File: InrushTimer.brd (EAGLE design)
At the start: 62.2 x 36 mm, 71 parts, among them IC1 TLC272D, IC2 555, IC3 4076N, Q2 TRANSISTOR-FET_2N7002, Q3 TRANSISTOR-FET_2N7002, Q4 TRANSISTOR-FET_2N7002, Q5 TRANSISTOR-FET_2N7002, Q6 DIODES_ZTX451DIODES_ZTX451_0_0, T1 MMBTA05, U1 ROHM_BY_ELEMENT14_BATCH_1_BU4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

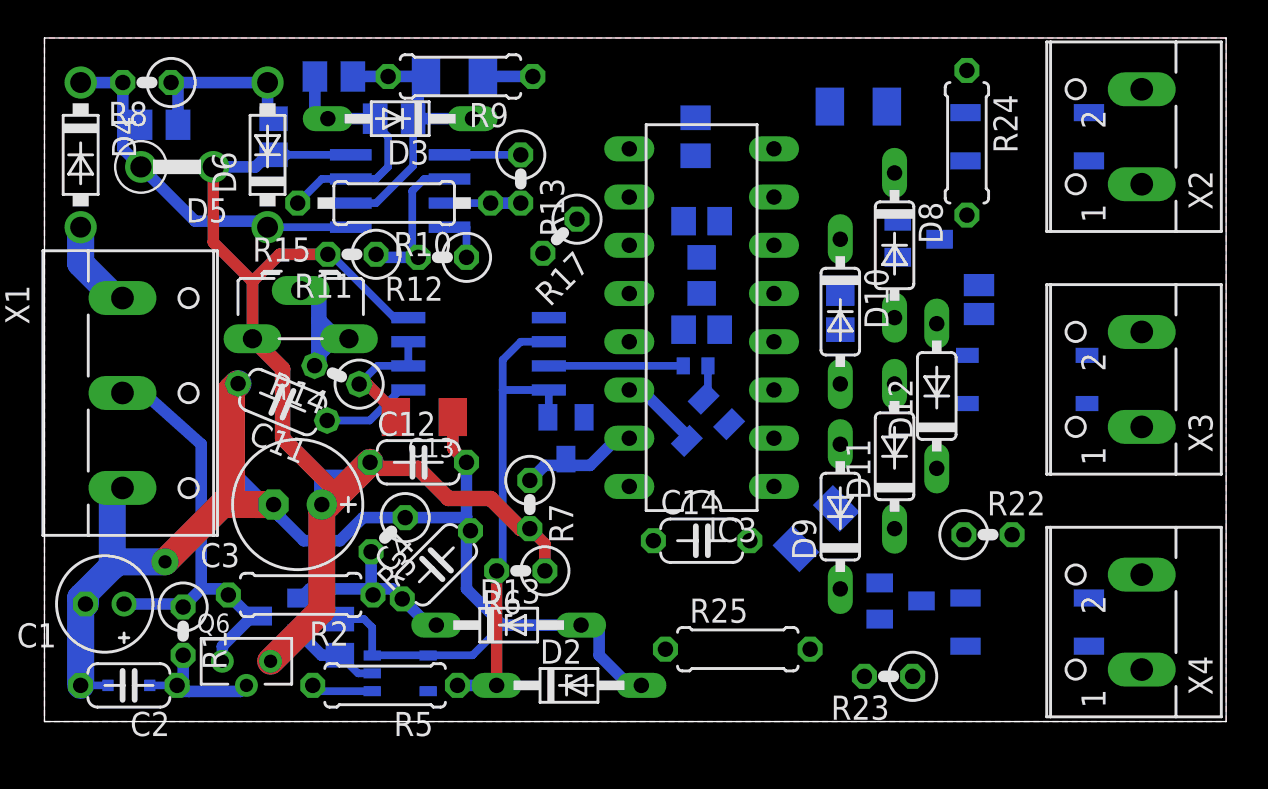
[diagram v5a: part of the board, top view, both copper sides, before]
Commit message: First complete routing fit. Passes design rules.
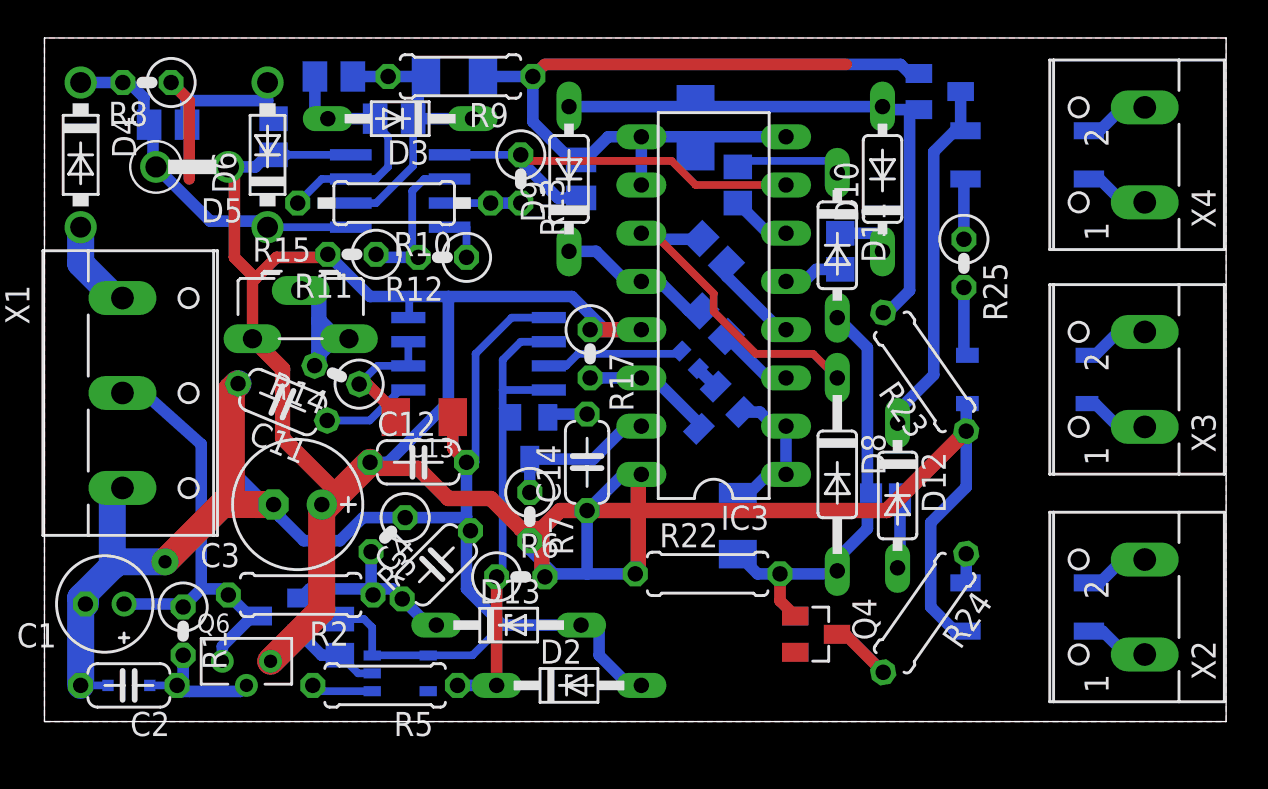
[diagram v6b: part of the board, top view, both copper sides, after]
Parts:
- D8: value 1N4148DO35-7 -> 1N4148DO35-10; device diode:DO35-7 -> diode:DO35-10
- R22, R23: device rcl:0207/2V -> rcl:0207/7
- R25: device rcl:0207/7 -> rcl:0207/2V
- moved Q5 26.9 mm to (47.1, 33.2)
- moved R24 24.9 mm to (46.4, 5.71), turned to 235 degrees
- moved X2 24.8 mm to (56.7, 6.03)
- moved OP1 24.8 mm to (51.8, 6.03)
- moved X4 24.6 mm to (56.7, 29.8)
- moved OP3 24.6 mm to (51.8, 29.8)
- moved R25 23.6 mm to (48.4, 24.1), turned to 270 degrees
- moved C15 23.0 mm to (36.5, 10.3), turned to 270 degrees
- moved D9 22.8 mm to (27.6, 28.6)
- moved C16 22.0 mm to (34.3, 31.3), turned to 270 degrees
- moved Q4 21.5 mm to (40.6, 4.60), flipped to the top, turned to 270 degrees
- moved R23 16.1 mm to (46.4, 18.4), turned to 125 degrees
- moved R22 14.9 mm to (34.9, 7.78)
- moved D8 12.4 mm to (41.8, 13.0)
- moved SJ1 11.6 mm to (44.3, 11.7), turned to 180 degrees
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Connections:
- net N$15: now also R25.1; no longer R25.2
- net N$16: now also IC3.12; no longer IC3.13
- net N$17: now also R25.2; no longer R25.1
- net N$20: now also X3.1; no longer X3.2
- net N$21: now also X3.2; no longer X3.1
- net N$22: now also R19.1; no longer R20.1
- net N$30: now also R20.1; no longer R19.1
- net RESET_N: now also R6.1; no longer R6.2
- net V12: now also IC3.13, R6.2; no longer IC3.12, R6.1
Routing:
- net ZERO: track 97.2 -> 181.3 mm
- net V12: track 87.6 -> 154.9 mm
- net ON_B_SYNC: track 0.00 -> 30.3 mm
- net ON_A_SYNC: track 0.00 -> 23.2 mm
- net N$6: track 0.00 -> 19.4 mm
- net PEAK: track 3.75 -> 22.7 mm
- net N$22: track 0.00 -> 17.5 mm
- net N$16: track 0.00 -> 8.25 mm
- net N$24: track 0.00 -> 6.01 mm
- net N$25: track 0.00 -> 4.94 mm
- net N$32: track 0.00 -> 4.04 mm
- net DISABLE_A: track 0.00 -> 3.70 mm
- net N$17: track 0.00 -> 3.65 mm
- net N$20: track 0.00 -> 3.55 mm
- net N$21: track 0.00 -> 3.55 mm
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
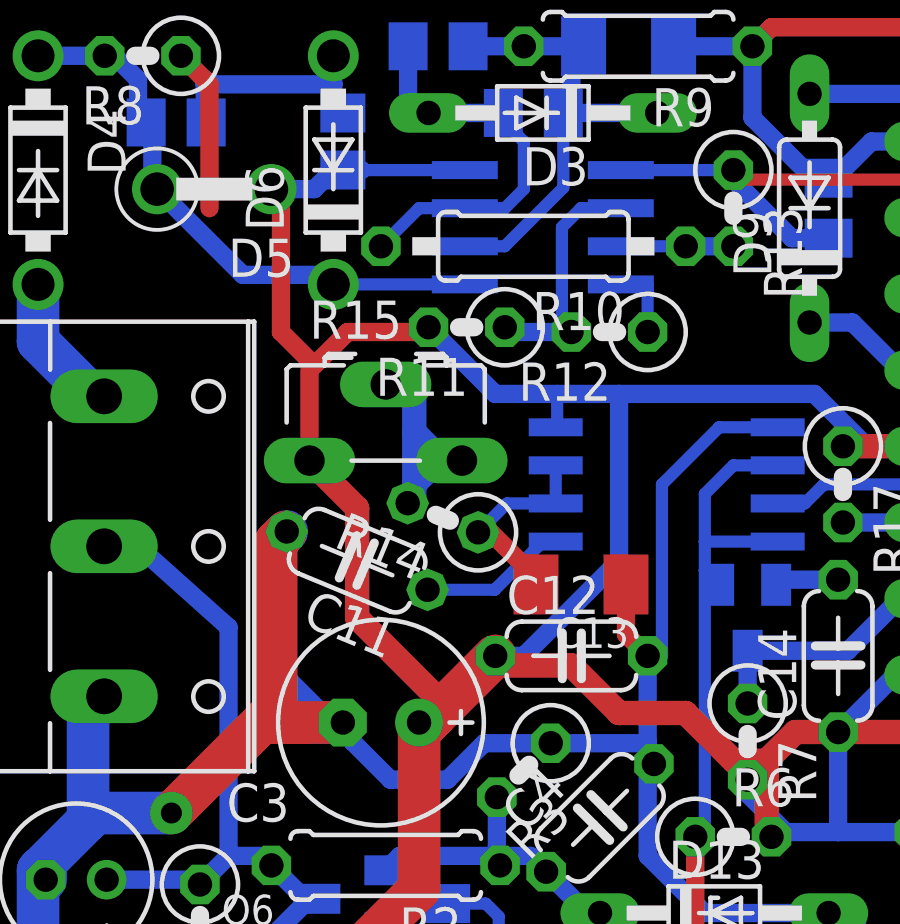
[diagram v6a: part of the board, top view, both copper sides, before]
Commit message: Slight track style tweaks.
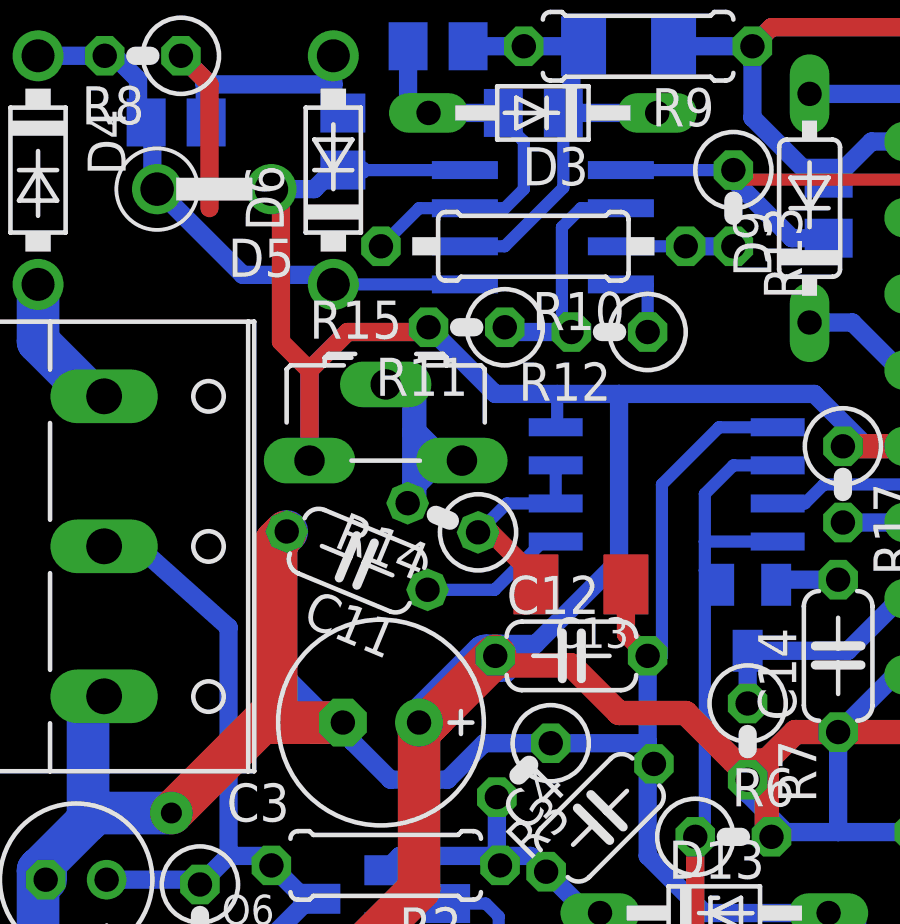
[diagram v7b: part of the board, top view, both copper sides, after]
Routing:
- net V12: track 154.9 -> 156.3 mm
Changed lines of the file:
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@@
 <layer number="39" name="tKeepout" color="4" fill="11" visible="no" active="yes"/>
 <layer number="40" name="bKeepout" color="1" fill="11" visible="no" active="yes"/>
-<layer number="41" name="tRestrict" color="4" fill="10" visible="no" active="yes"/>
+<layer number="41" name="tRestrict" color="4" fill="10" visible="yes" active="yes"/>
 <layer number="42" name="bRestrict" color="1" fill="10" visible="yes" active="yes"/>
 <layer number="43" name="vRestrict" color="2" fill="10" visible="no" active="yes"/>
@@
 <rectangle x1="49.53" y1="0" x2="62.23" y2="36" layer="42"/>
 <rectangle x1="49.53" y1="0" x2="62.23" y2="36" layer="41"/>
-<rectangle x1="0" y1="20.0025" x2="6.35" y2="36" layer="41"/>
+<rectangle x1="0" y1="19.05" x2="6.35" y2="36" layer="41"/>
 <rectangle x1="0" y1="19.05" x2="9.144" y2="30.48" layer="42"/>
 </plain>
@@
 <wire x1="14.605" y1="11.1125" x2="14.9225" y2="11.43" width="1.4224" layer="1"/>
 <wire x1="14.9225" y1="11.43" x2="15.08125" y2="11.58875" width="1.4224" layer="1"/>
-<wire x1="15.08125" y1="11.58875" x2="15.478125" y2="11.985625" width="1.4224" layer="1"/>
-<wire x1="15.478125" y1="11.985625" x2="17.145" y2="13.6525" width="1.4224" layer="1"/>
+<wire x1="15.08125" y1="11.58875" x2="17.145" y2="13.6525" width="1.4224" layer="1"/>
 <wire x1="14.605" y1="11.43" x2="14.9225" y2="11.43" width="1.4224" layer="1"/>
 <wire x1="14.76375" y1="11.58875" x2="15.08125" y2="11.58875" width="0.6096" layer="1"/>
 <contactref element="R15" pad="A"/>
-<wire x1="12.54125" y1="18.57375" x2="12.54125" y2="14.9225" width="0.8128" layer="1"/>
-<wire x1="12.54125" y1="14.9225" x2="15.478125" y2="11.985625" width="0.8128" layer="1"/>
 <contactref element="R7" pad="2"/>
-<wire x1="10.95375" y1="20.16125" x2="12.54125" y2="18.57375" width="0.8128" layer="1"/>
 <wire x1="15.08125" y1="24.60625" x2="14.9225" y2="24.60625" width="0.4064" layer="16"/>
 <wire x1="17.145" y1="13.6525" x2="17.4625" y2="13.335" width="0.8128" layer="1"/>
@@
 <wire x1="31.4325" y1="20.6375" x2="28.73375" y2="20.6375" width="0.8128" layer="1"/>
 <wire x1="21.2725" y1="16.8275" x2="21.2725" y2="22.38375" width="0.6096" layer="16"/>
-<wire x1="21.2725" y1="16.8275" x2="18.0975" y2="13.6525" width="0.6096" layer="16"/>
-<wire x1="14.605" y1="11.43" x2="16.8275" y2="13.6525" width="0.8128" layer="16"/>
-<wire x1="18.0975" y1="13.6525" x2="17.145" y2="13.6525" width="0.6096" layer="16"/>
+<wire x1="21.2725" y1="16.8275" x2="18.494375" y2="14.049375" width="0.6096" layer="16"/>
 <wire x1="48.540325" y1="12.345325" x2="46.6725" y2="10.4775" width="0.6096" layer="16"/>
 <wire x1="46.6725" y1="6.0325" x2="47.9425" y2="4.7625" width="0.6096" layer="16"/>
@@
 <wire x1="25.0825" y1="10.16" x2="26.19375" y2="10.16" width="0.8128" layer="1"/>
 <wire x1="9.68375" y1="29.21" x2="10.00125" y2="29.21" width="0.6096" layer="1"/>
-<wire x1="10.00125" y1="29.21" x2="10.00125" y2="24.4475" width="0.6096" layer="1"/>
+<wire x1="10.00125" y1="29.21" x2="10.00125" y2="24.13" width="0.6096" layer="1"/>
 <wire x1="14.9225" y1="24.60625" x2="14.76375" y2="24.4475" width="0.6096" layer="1"/>
 <wire x1="14.76375" y1="24.4475" x2="12.22375" y2="24.4475" width="0.6096" layer="1"/>
-<wire x1="12.22375" y1="24.4475" x2="11.1125" y2="23.33625" width="0.6096" layer="1"/>
-<wire x1="10.00125" y1="24.4475" x2="11.1125" y2="23.33625" width="0.6096" layer="1"/>
+<wire x1="12.22375" y1="24.4475" x2="10.95375" y2="23.1775" width="0.6096" layer="1"/>
 <wire x1="10.95375" y1="23.1775" x2="10.95375" y2="20.16125" width="0.6096" layer="1"/>
+<wire x1="14.9225" y1="24.60625" x2="14.76375" y2="24.4475" width="0.6096" layer="16"/>
+<wire x1="14.76375" y1="24.4475" x2="12.22375" y2="24.4475" width="0.6096" layer="16"/>
+<wire x1="10.95375" y1="23.1775" x2="10.95375" y2="20.16125" width="0.6096" layer="16"/>
+<wire x1="16.8275" y1="13.6525" x2="17.30375" y2="13.6525" width="1.4224" layer="16"/>
+<wire x1="16.98625" y1="14.049375" x2="18.494375" y2="14.049375" width="0.6096" layer="16"/>
+<wire x1="18.494375" y1="14.049375" x2="17.541875" y2="13.096875" width="0.6096" layer="16"/>
+<wire x1="17.541875" y1="13.096875" x2="17.30375" y2="13.096875" width="0.6096" layer="16"/>
+<wire x1="17.30375" y1="13.096875" x2="16.271875" y2="13.096875" width="0.6096" layer="16"/>
+<wire x1="16.8275" y1="13.6525" x2="14.605" y2="11.43" width="1.4224" layer="16"/>
+<wire x1="10.00125" y1="24.13" x2="10.95375" y2="23.1775" width="0.6096" layer="1"/>
+<wire x1="12.22375" y1="24.4475" x2="10.95375" y2="23.1775" width="0.6096" layer="16"/>
+<wire x1="17.30375" y1="13.6525" x2="17.30375" y2="13.096875" width="0.6096" layer="16"/>
 </signal>
 <signal name="ZERO">

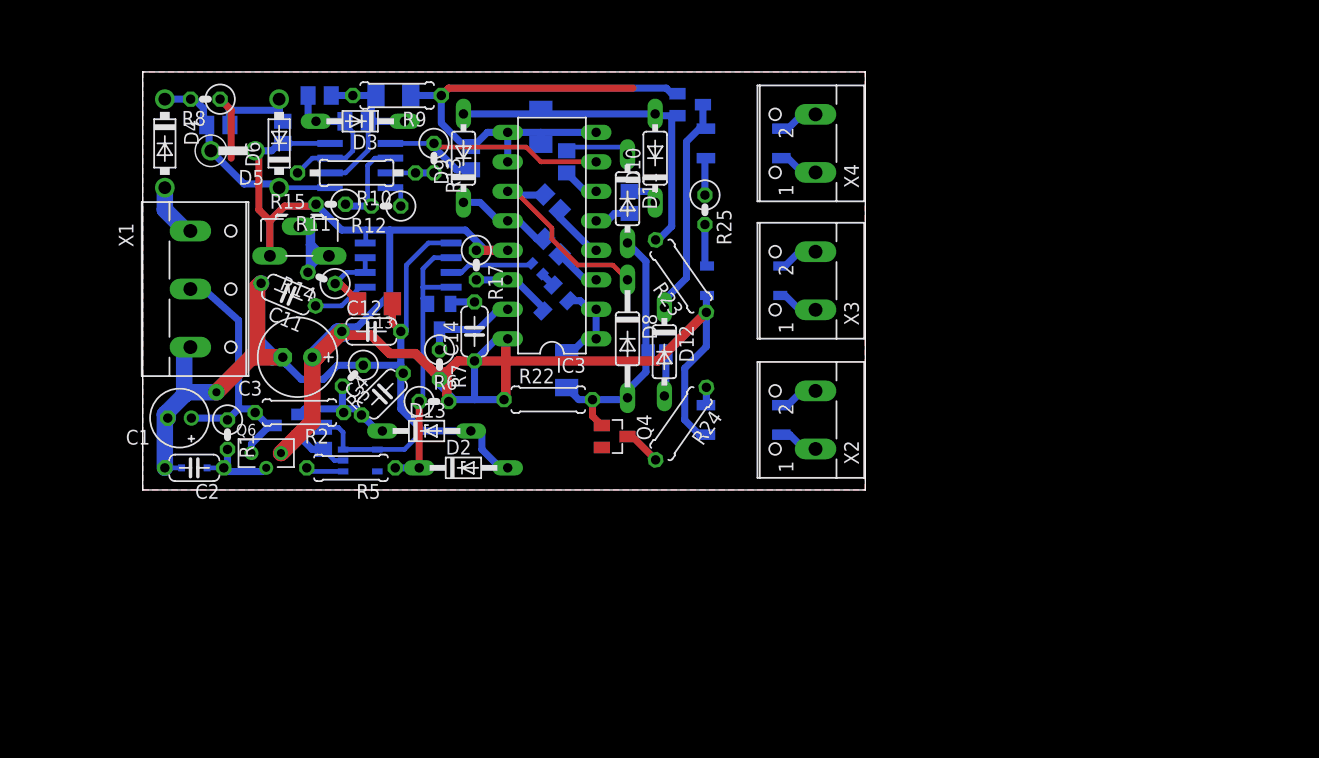
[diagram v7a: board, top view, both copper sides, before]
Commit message: Pushed some tracks to the bottom side
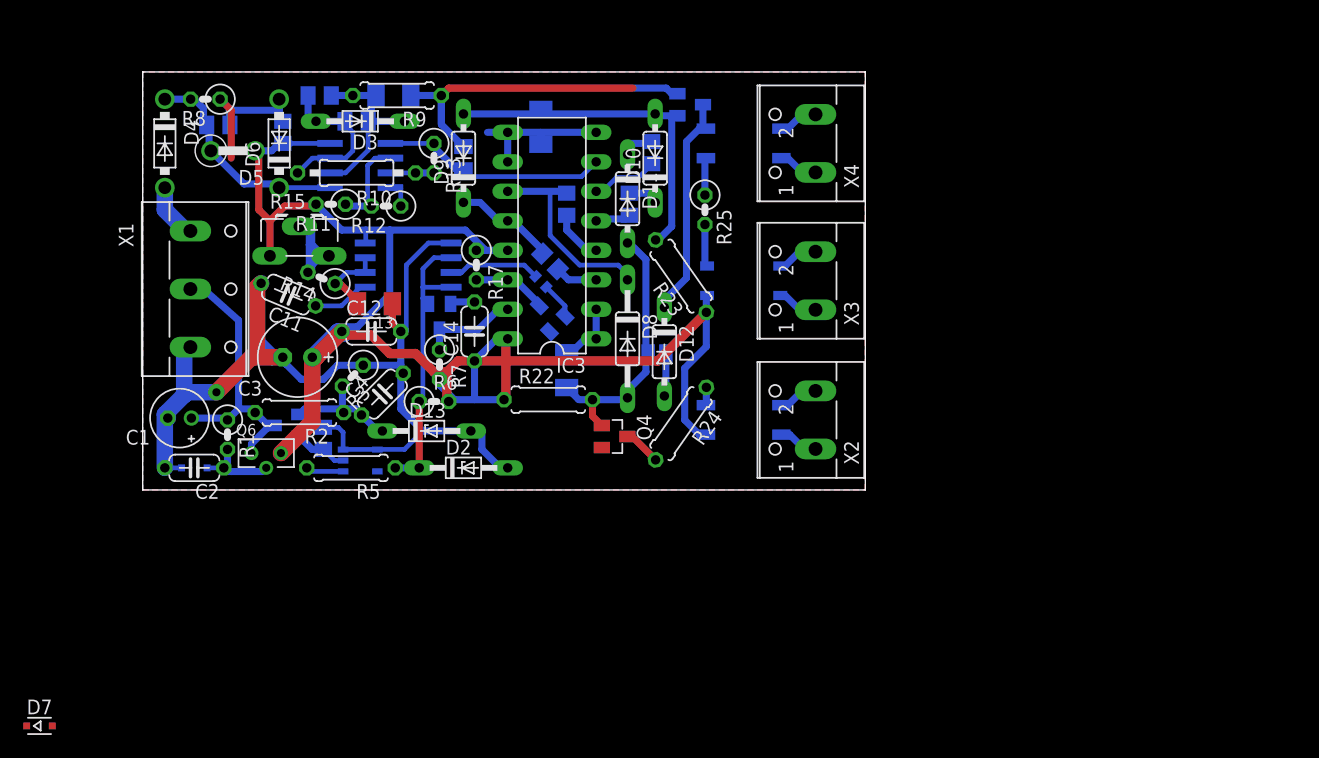
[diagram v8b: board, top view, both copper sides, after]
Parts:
- added D7: (no value), diode:SOD323-R
- R25: value 1K -> 1K5
- moved R21 7.35 mm to (43.8, 29.1)
- moved R19 1.28 mm to (36.5, 24.6), turned to 270 degrees
- moved R18 1.28 mm to (35.1, 19.7)
- moved R16 1.16 mm to (34.3, 17.9)
- moved Q3 1.16 mm to (34.9, 15.1), turned to 315 degrees
- moved C10 0.64 mm to (27.6, 28.6)
- moved R20 0.16 mm to (41.9, 24.6)
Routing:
- net N$24: track 6.01 -> 3.08 mm
- net PEAK: track 22.7 -> 19.8 mm
- net ZERO: track 181.3 -> 178.5 mm
- net V12: track 156.3 -> 153.6 mm
- net N$3: track 3.20 -> 5.80 mm
- net N$36: track 1.65 -> 3.18 mm
- net N$48: track 7.27 -> 7.93 mm
- net ON_B: track 7.01 -> 6.43 mm
- net N$16: track 8.25 -> 8.80 mm
